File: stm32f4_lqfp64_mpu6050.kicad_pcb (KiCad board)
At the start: 4 copper layers, 130 x 100 mm, 172 parts, among them M5 ALIS-CUSTOM-PARTS_POWERPADS, P1 CONN_01X08, P2 CONN_02X08, Q5 BSS138, Q6 CRYSTAL_50X32, U1 STM32F405R, U2 MPU6050, U3 LP2985LV, U4 LP2985LV, U5 W25Q80BV, U6 LM1881, U7 TS5A3160, U8 TS5A3160, X1 CON-JST_SM04B-SRSS-TB, X2 CON-JST_SM04B-SRSS-TB, X4 CON-JST_SM04B-SRSS-TB

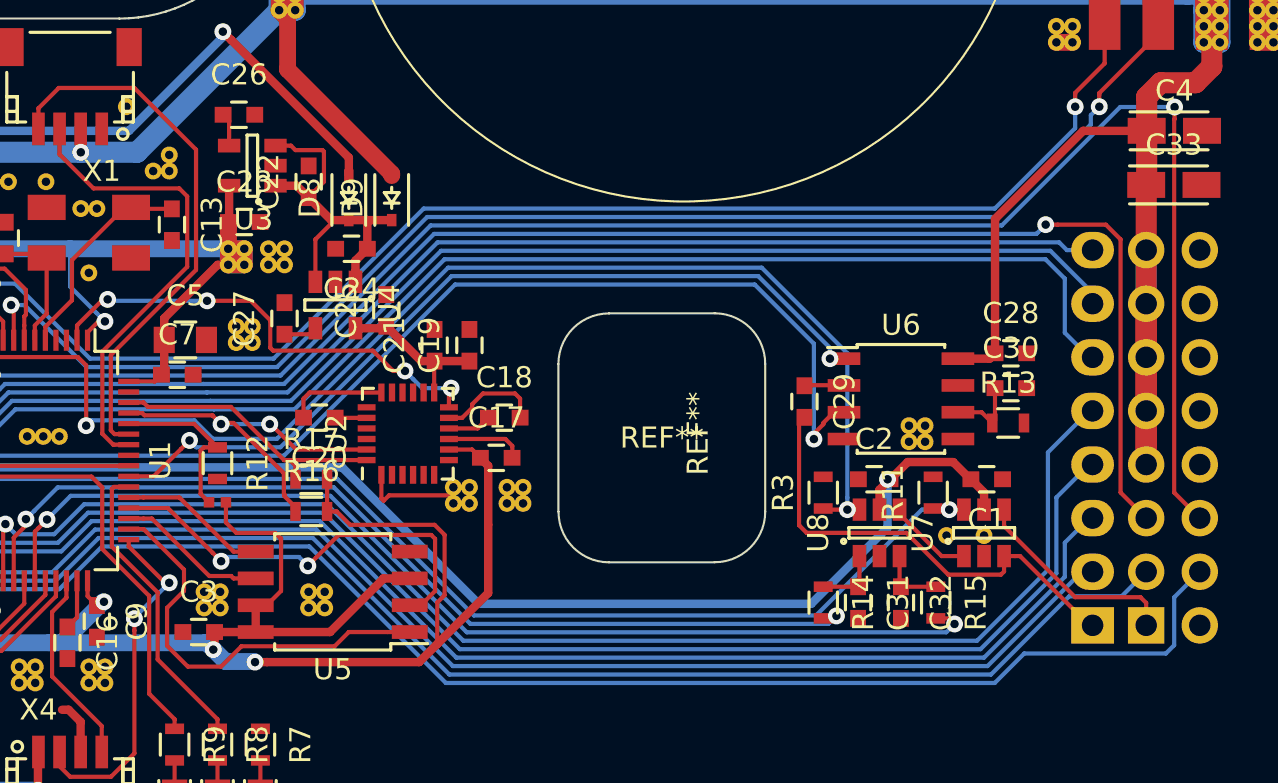
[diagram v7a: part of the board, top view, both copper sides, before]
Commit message: added lt6206 and replaced lm1881 with lmh1980. routing unfinished.
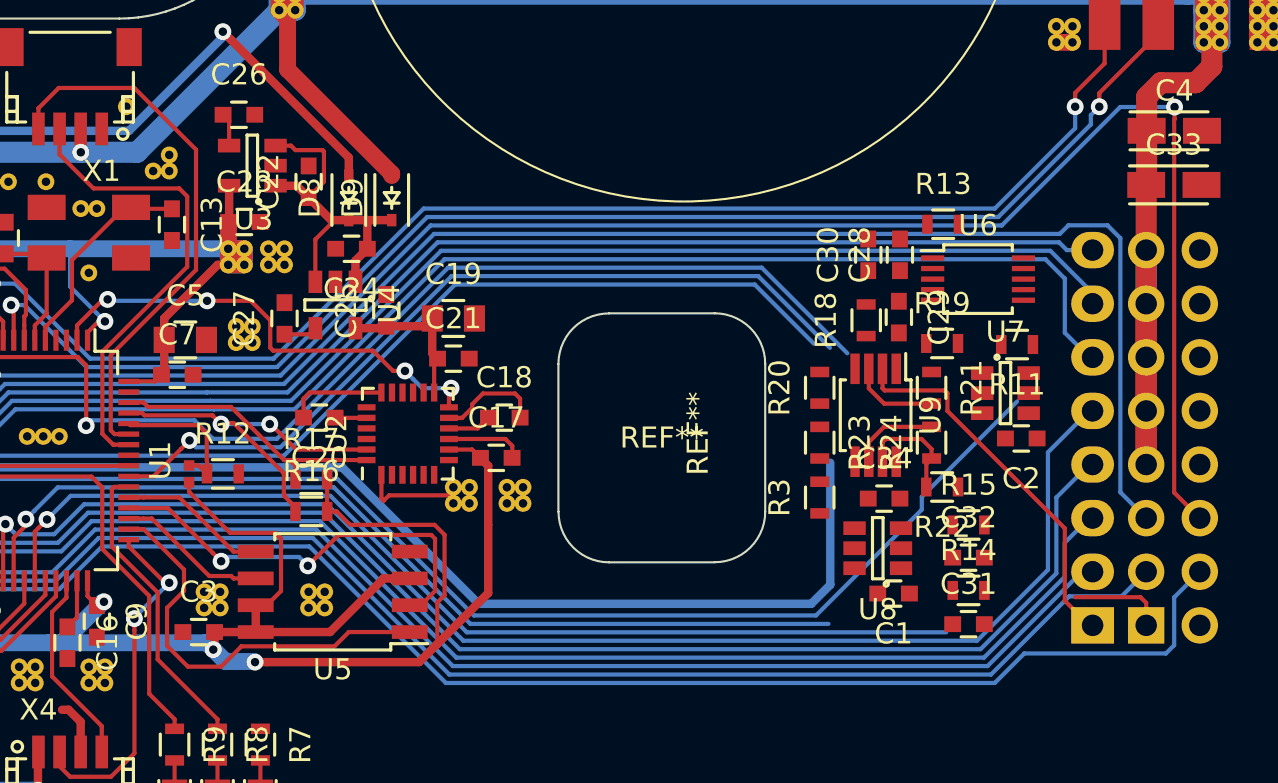
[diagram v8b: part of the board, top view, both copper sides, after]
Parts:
- removed the ? at (155.8, 105.2)
- removed the ? at (155.8, 104.4)
- removed the ? at (156.6, 105.2)
- removed the ? at (156.6, 104.4)
- removed the ? at (159.4, 109.6)
- removed the ? at (157.6, 109.6)
- added C34: 100n, Capacitors_SMD:C_0603, F.Cu at (154.7, 107.8)
- added R18: 75R, Resistors_SMD:R_0603, F.Cu at (153.8, 99.4)
- added R19: 75R, Resistors_SMD:R_0603, F.Cu at (157.4, 100.5)
- added R20: 490R, Resistors_SMD:R_0603, F.Cu at (151.6, 102.6)
- added R21: 490R, Resistors_SMD:R_0603, F.Cu at (156.9, 102.6)
- added R22: 75R, Resistors_SMD:R_0603, F.Cu at (157.4, 107.3)
- added R23: 490R, Resistors_SMD:R_0603, F.Cu at (151.6, 105.2)
- added R24: 490R, Resistors_SMD:R_0603, F.Cu at (156.9, 105.2)
- added U9: LT6206, Housings_SSOP:MSOP-8_3x3mm_Pitch0.65mm, F.Cu at (154.2, 103.9)
- C19: footprint Capacitors_SMD:C_0603 -> Capacitors_SMD:C_0805
- R13: value 680k -> 10k 1%
- U6: value LM1881 -> LMH1980; footprint Housings_SOIC:SOIC-8_3.9x4.9mm_Pitch1.27mm -> Housings_SSOP:TSSOP-10_3x3mm_Pitch0.5mm
- moved R13 9.91 mm to (157.4, 94.8)
- moved C30 9.25 mm to (153.9, 96.3), turned to 90 degrees
- moved R11 8.07 mm to (160.9, 100.5), turned to 180 degrees
- moved C2 7.24 mm to (161.2, 105.0), turned to 180 degrees
- moved C28 7.03 mm to (155.4, 96.3), turned to 90 degrees
- moved C1 6.99 mm to (155.1, 112.3)
- moved R14 6.91 mm to (158.7, 112.2), turned to 0 degrees
- moved U6 6.75 mm to (159.1, 97.5)
- moved U7 6.70 mm to (160.4, 102.8), turned to 0 degrees
- moved C29 6.00 mm to (155.3, 99.2)
- moved C31 5.33 mm to (158.7, 113.8), turned to 0 degrees
- moved R15 3.99 mm to (158.7, 109.1), turned to 0 degrees
- moved C32 3.84 mm to (158.7, 110.7), turned to 0 degrees
- moved JP2 1.98 mm to (121.7, 106.7), turned to 90 degrees
- moved C19 1.48 mm to (134.2, 99.3), turned to 0 degrees
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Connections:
- C28 pad 1: VBAT -> Net-(C28-Pad1)
- C29 pad 2: VIDEO_IN -> Net-(C29-Pad2)
- R13 pad 1: Net-(C30-Pad1) -> Net-(R13-Pad1)
- R14 pad 2: B_PWM -> W_PWM
- R15 pad 2: W_PWM -> B_PWM
- U6 pad 1: HSYNC_CAPT -> Net-(R13-Pad1)
- U6 pad 2: Net-(C29-Pad1) -> GND
- U6 pad 3: VSYNC_EXTI -> Net-(C30-Pad1)
- U6 pad 4: GND -> Net-(C29-Pad1)
- U6 pad 6: Net-(C30-Pad1) -> HSYNC_CAPT
- U6 pad 7: Net-(U6-Pad7) -> VSYNC_EXTI
- U6 pad 8: VBAT -> Net-(U6-Pad8)
- U7 pad 1: Net-(U7-Pad1) -> Net-(R19-Pad2)
- U7 pad 3: VIDEO_IN -> Net-(R22-Pad1)
- U8 pad 4: Net-(U7-Pad1) -> Net-(U8-Pad4)
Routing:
- net VBAT: track 170.3 -> 153.2 mm
- net BW_LEVEL: track 58.9 -> 49.8 mm, vias 2 -> 1
- net VSYNC_EXTI: track 55.3 -> 48.6 mm, vias 2 -> 1
- net 3.3V: track 265.0 -> 258.7 mm, vias 8 -> 7
- net VIDEO_OUT: track 10.1 -> 4.54 mm
- net Net-(R22-Pad2): track 0.00 -> 5.41 mm
- net VIDEO_IN: track 22.2 -> 18.0 mm
- net Net-(R23-Pad1): track 0.00 -> 4.20 mm
- net Net-(R20-Pad1): track 0.00 -> 4.20 mm
- net BW_MASK: track 60.3 -> 64.4 mm, vias 2 -> 1
- net Net-(U7-Pad1): track 4.08 -> 0.00 mm
- net Net-(C30-Pad1): track 3.54 -> 0.00 mm
- net Net-(C31-Pad1): track 3.13 -> 0.00 mm
- net Net-(C32-Pad1): track 3.13 -> 0.00 mm
- net Net-(C29-Pad1): track 1.88 -> 0.00 mm
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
